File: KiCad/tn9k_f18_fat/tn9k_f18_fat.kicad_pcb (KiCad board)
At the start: 2 copper layers, 43.2 x 64.8 mm, 9 parts, among them J1 Conn_01x20, J2 Conn_01x20, J3 Conn_01x24, J4 Conn_01x24, J5 Conn_02x04_Counter_Clockwise, J6 Conn_02x08_Odd_Even, U1 SN74LVC245, U2 SN74LVC245, U3 SN74LVC245

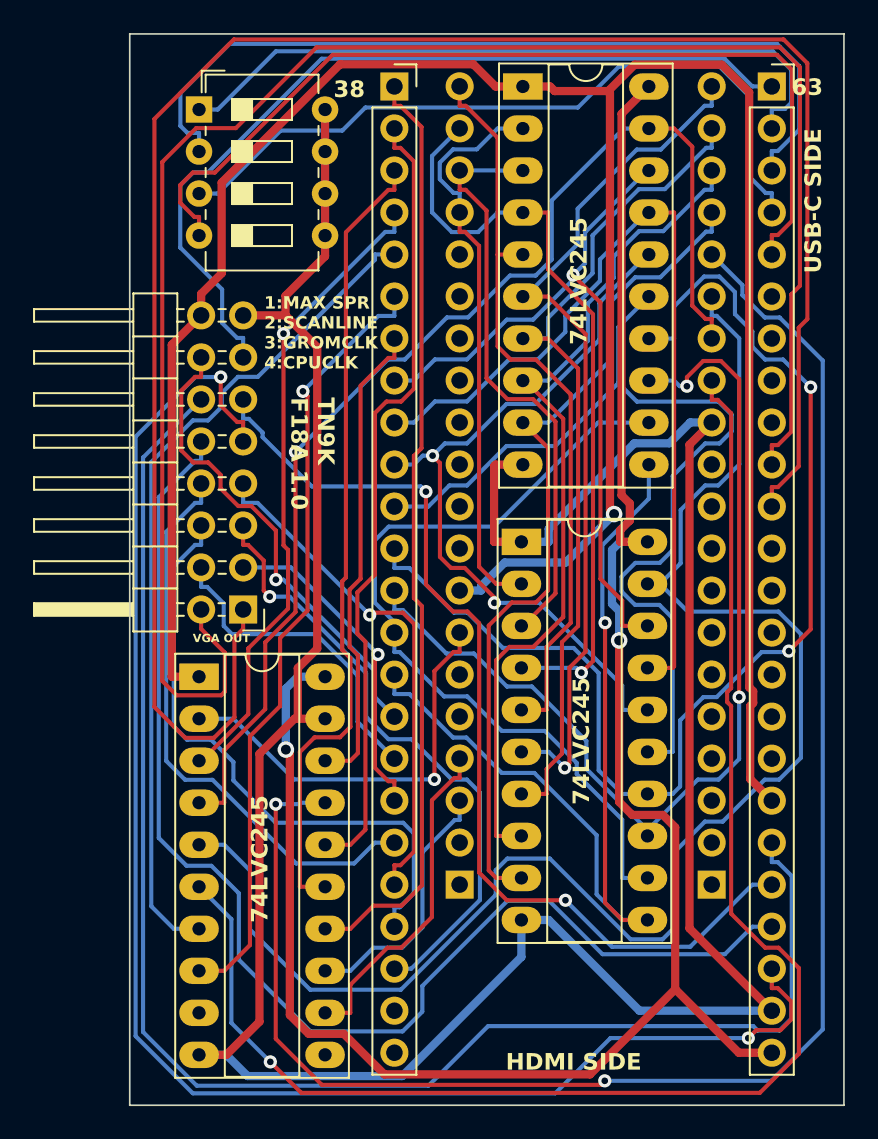
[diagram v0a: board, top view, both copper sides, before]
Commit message: update silk on fat board
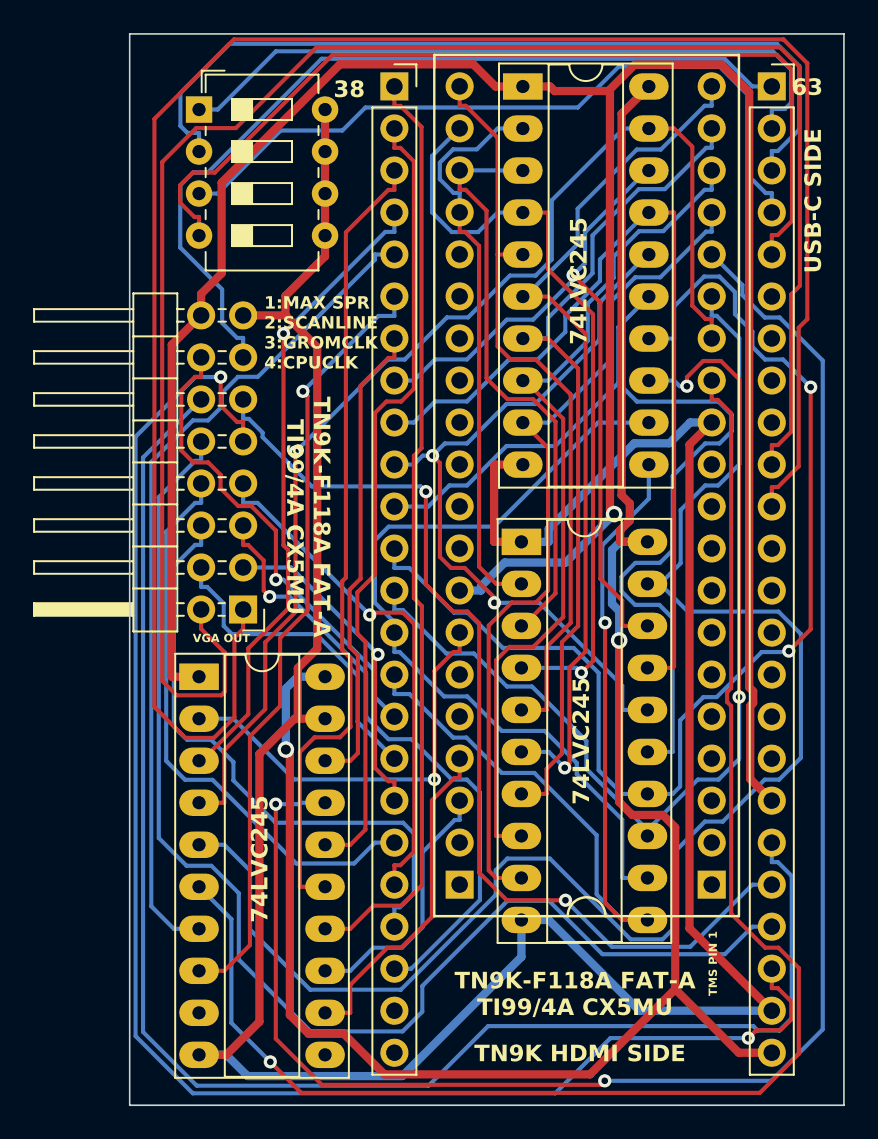
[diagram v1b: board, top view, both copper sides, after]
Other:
- board text added: "TMS PIN 1"
- board text added: "TN9K HDMI SIDE"
- board text added: "TN9K-F118A FAT-A TI99/4A CX5MU"
- board text removed: "HDMI SIDE"
- board text removed: "TN9K F18A 1.0"
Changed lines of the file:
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@@
     )
   )
+  (gr_line (start 153.035 48.26) (end 171.45 48.26)
+    (stroke (width 0.15) (type default)) (layer "F.SilkS"))
+  (gr_line (start 153.035 48.26) (end 153.035 100.33)
+    (stroke (width 0.15) (type default)) (layer "F.SilkS"))
+  (gr_line (start 153.035 100.33) (end 171.45 100.33)
+    (stroke (width 0.15) (type default)) (layer "F.SilkS"))
+  (gr_arc (start 161.097738 100.33) (mid 162.2425 99.185238) (end 163.387262 100.33)
+    (stroke (width 0.15) (type default)) (layer "F.SilkS"))
+  (gr_line (start 171.45 48.26) (end 171.45 100.33)
+    (stroke (width 0.15) (type default)) (layer "F.SilkS"))
   (gr_line (start 177.8 46.99) (end 177.8 111.76)
     (stroke (width 0.1) (type default)) (layer "Edge.Cuts"))
@@
     (effects (font (size 1 1) (thickness 0.25) bold) (justify left bottom))
   )
-  (gr_text "TN9K\nF18A 1.0" (at 144.272 68.961 -90) (layer "F.SilkS")
-    (effects (font (size 1 1) (thickness 0.25) bold) (justify left bottom))
-  )
   (gr_text "1:MAX SPR\n2:SCANLINE\n3:GROMCLK\n4:CPUCLK" (at 142.748 67.31) (layer "F.SilkS")
     (effects (font (size 0.75 0.75) (thickness 0.1875) bold) (justify left bottom))
@@
   (gr_text "74LVC245" (at 143.0682 100.7314 90) (layer "F.SilkS")
     (effects (font (size 1 1) (thickness 0.25) bold) (justify left bottom))
+  )
+  (gr_text "TN9K-F118A FAT-A \nTI99/4A CX5MU" (at 161.544 106.426) (layer "F.SilkS")
+    (effects (font (size 1 1) (thickness 0.25) bold) (justify bottom))
   )
   (gr_text "USB-C SIDE" (at 176.53 61.468 90) (layer "F.SilkS")
@@
     (effects (font (size 0.5 0.5) (thickness 0.125) bold) (justify left bottom))
   )
-  (gr_text "HDMI SIDE" (at 157.353 109.728) (layer "F.SilkS")
+  (gr_text "TN9K HDMI SIDE" (at 155.448 109.22) (layer "F.SilkS")
     (effects (font (size 1 1) (thickness 0.25) bold) (justify left bottom))
   )
@@
     (effects (font (size 1 1) (thickness 0.25) bold) (justify left bottom))
   )
+  (gr_text "TN9K-F118A FAT-A \nTI99/4A CX5MU" (at 144.018 76.2 -90) (layer "F.SilkS")
+    (effects (font (size 1 1) (thickness 0.25) bold) (justify bottom))
+  )
   (gr_text "63" (at 174.625 50.8) (layer "F.SilkS")
     (effects (font (size 1 1) (thickness 0.25) bold) (justify left bottom))
   )
+  (gr_text "TMS PIN 1" (at 170.18 105.156 90) (layer "F.SilkS")
+    (effects (font (size 0.5 0.5) (thickness 0.125) bold) (justify left bottom))
+  )
   (dimension (type aligned) (layer "User.1")

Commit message: update FAT board for the diode
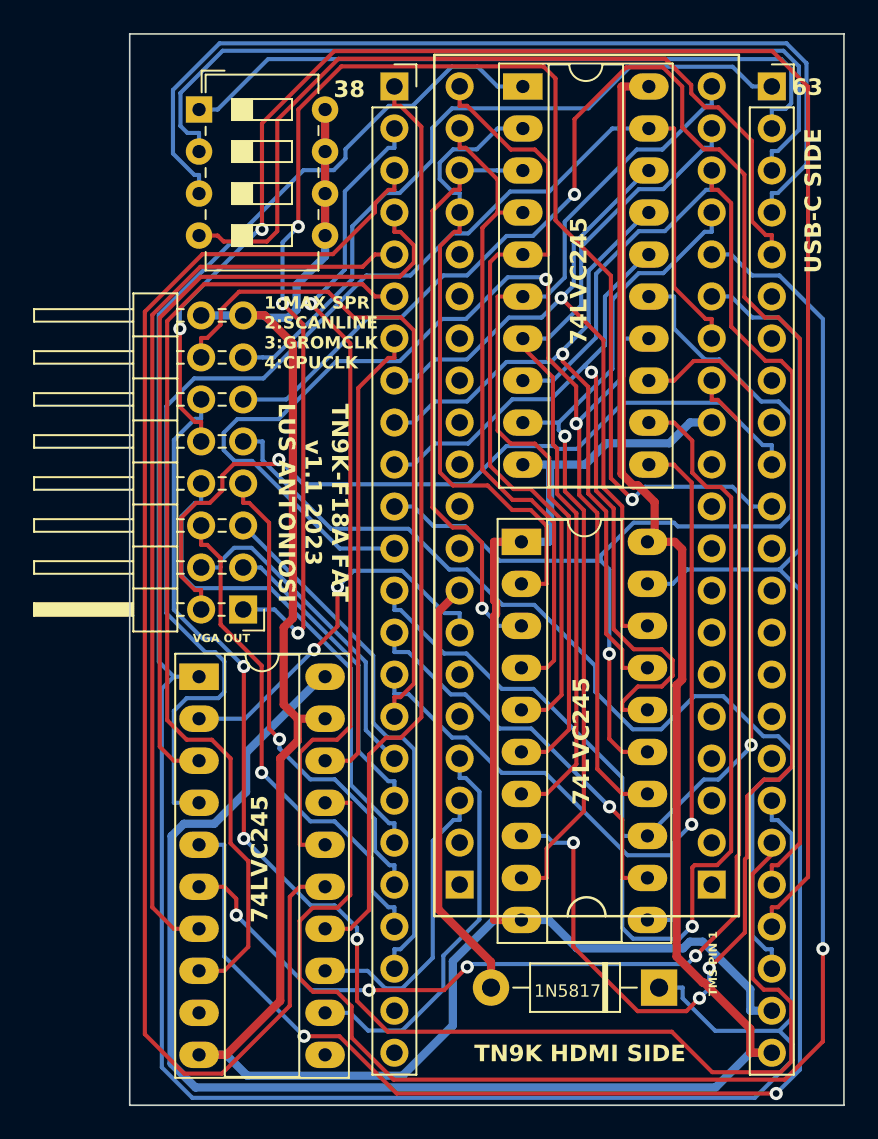
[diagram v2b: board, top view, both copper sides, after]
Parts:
- added D1: 1N5817, Diode_THT:D_DO-41_SOD81_P10.16mm_Horizontal, F.Cu at (166.6, 104.6)
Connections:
- J4 pad 18: VCC -> VDD
- J6 pad 16: VCC -> GND
- U2 pad 1: VCC -> VDD
- U3 pad 1: VCC -> VDD
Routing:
- net VDD: track 0.00 -> 142.4 mm
- net VCC: track 150.3 -> 25.9 mm, vias 1 -> 0
- net R1_3V3: track 108.0 -> 49.0 mm, vias 0 -> 1
- net CD6: track 52.1 -> 94.5 mm, vias 0 -> 3
- net ~{CSR_3V3}: track 48.7 -> 83.7 mm
- net B0_3V3: track 94.2 -> 59.6 mm, vias 2 -> 0
- net B1_3V3: track 75.7 -> 109.8 mm, vias 0 -> 2
- net B2_3V3: track 60.2 -> 91.1 mm, vias 2 -> 1
- net R0_3V3: track 118.4 -> 90.2 mm, vias 0 -> 4
- net CD6_3V3: track 50.2 -> 69.2 mm, vias 0 -> 2
- net MODE: track 89.9 -> 70.8 mm, vias 1 -> 4
- net VCC_3V3: track 118.7 -> 132.4 mm, vias 2 -> 0
- net ~{CSR}: track 94.2 -> 107.0 mm, vias 0 -> 2
- net USR3_1V8: track 45.0 -> 57.2 mm
- net GROMCLK_3V3: track 47.3 -> 59.3 mm, vias 1 -> 0
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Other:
- board text added: "TN9K-F18A FAT v1.1 2023 LUS ANTONIOSI"
- board text removed: "TN9K-F118A FAT-A TI99/4A CX5MU"
